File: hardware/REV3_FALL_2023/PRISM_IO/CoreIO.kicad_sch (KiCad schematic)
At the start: 30 parts, among them J1 CORE_FC, J2 COTS_SWITCH_PLUG, J3 PYRO 1, J4 PYRO 2, Q1 AO3400A, Q2 AO3400A

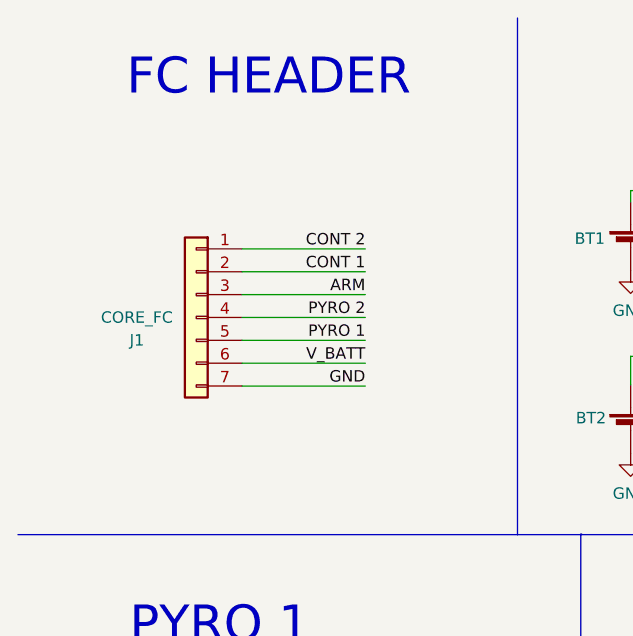
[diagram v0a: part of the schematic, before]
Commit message: added teensy 4.0 and new connector spec
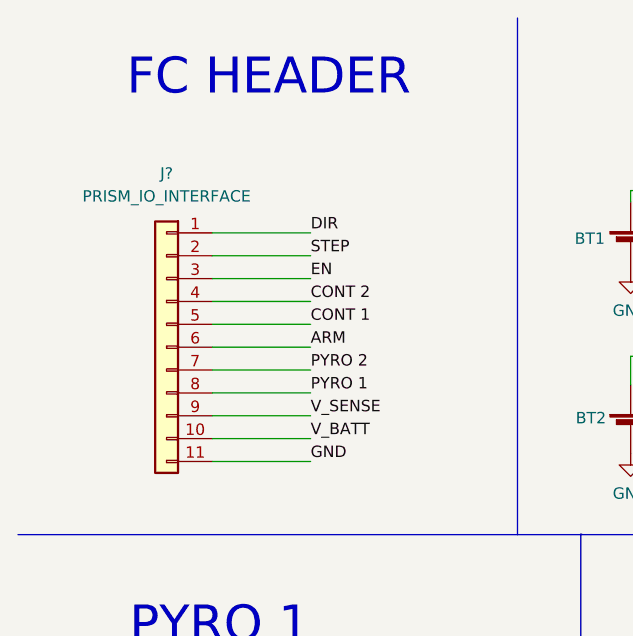
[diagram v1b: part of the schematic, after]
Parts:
- removed J1: CORE_FC, Connector_JST:JST_PH_S7B-PH-K_1x07_P2.00mm_Horizontal, symbol Connector_Generic:Conn_01x07
- added J?: PRISM_IO_INTERFACE, symbol Connector_Generic:Conn_01x11
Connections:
- net ARM: now also J?.6 (Pin_6)
- net CONT 1: now also J?.5 (Pin_5)
- net CONT 2: now also J?.4 (Pin_4)
- net GND: now also J?.11 (Pin_11)
- net PYRO 1: now also J?.8 (Pin_8)
- net PYRO 2: now also J?.7 (Pin_7)
- net V_BATT: now also J?.10 (Pin_10)
- new net DIR: J?.1 (Pin_1)
- new net EN: J?.3 (Pin_3)
- new net STEP: J?.2 (Pin_2)
- new net V_SENSE: J?.9 (Pin_9)
